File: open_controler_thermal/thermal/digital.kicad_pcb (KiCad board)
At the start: 2 copper layers, 56 x 85 mm, 6 parts, among them J1 d_o_01x10, J2 d_i_01x10, J3 Conn_02x20_Odd_Even, J4 Conn_01x02

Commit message: trabajando en openControllerDigital
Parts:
- removed the J1 at (75.7, 82.8)
- added C1: 10nF, Capacitor_SMD:C_1206_3216Metric_Pad1.42x1.75mm_HandSolder, F.Cu at (109.0, 138.3)
- added C10: 10nF, Capacitor_SMD:C_1206_3216Metric_Pad1.42x1.75mm_HandSolder, F.Cu at (85.4, 74.2)
- added C11: 10nF, Capacitor_SMD:C_1206_3216Metric_Pad1.42x1.75mm_HandSolder, F.Cu at (90.0, 62.2)
- added C12: 10nF, Capacitor_SMD:C_1206_3216Metric_Pad1.42x1.75mm_HandSolder, F.Cu at (94.7, 74.1)
- added C13: 10nF, Capacitor_SMD:C_1206_3216Metric_Pad1.42x1.75mm_HandSolder, F.Cu at (99.2, 62.2)
- added C14: 10nF, Capacitor_SMD:C_1206_3216Metric_Pad1.42x1.75mm_HandSolder, F.Cu at (104.0, 74.2)
- added C15: 10nF, Capacitor_SMD:C_1206_3216Metric_Pad1.42x1.75mm_HandSolder, F.Cu at (108.5, 62.2)
- added C16: 10nF, Capacitor_SMD:C_1206_3216Metric_Pad1.42x1.75mm_HandSolder, F.Cu at (113.0, 74.2)
- added C2: 10nF, Capacitor_SMD:C_1206_3216Metric_Pad1.42x1.75mm_HandSolder, F.Cu at (79.3, 92.5)
- added C3: 10nF, Capacitor_SMD:C_1206_3216Metric_Pad1.42x1.75mm_HandSolder, F.Cu at (79.4, 97.8)
- added C4: 10nF, Capacitor_SMD:C_1206_3216Metric_Pad1.42x1.75mm_HandSolder, F.Cu at (79.4, 103.2)
- added C5: 10nF, Capacitor_SMD:C_1206_3216Metric_Pad1.42x1.75mm_HandSolder, F.Cu at (79.4, 113.9)
- added C6: 10nF, Capacitor_SMD:C_1206_3216Metric_Pad1.42x1.75mm_HandSolder, F.Cu at (79.4, 119.3)
- added C8: 10nF, Capacitor_SMD:C_1206_3216Metric_Pad1.42x1.75mm_HandSolder, F.Cu at (79.4, 108.5)
- added C9: 10nF, Capacitor_SMD:C_1206_3216Metric_Pad1.42x1.75mm_HandSolder, F.Cu at (79.3, 130.0)
- added J4: e_i_01x10, Connector_Phoenix_MC:PhoenixContact_MCV_1,5_10-G-3.5_1x10_P3.50mm_Vertical, F.Cu at (72.7, 98.4)
- added JP1: 23, Jumper:SolderJumper-2_P1.3mm_Open_RoundedPad1.0x1.5mm, F.Cu at (111.5, 96.8)
- added JP2: 19, Jumper:SolderJumper-2_P1.3mm_Open_RoundedPad1.0x1.5mm, F.Cu at (111.5, 112.0)
- added JP3: 18, Jumper:SolderJumper-2_P1.3mm_Open_RoundedPad1.0x1.5mm, F.Cu at (111.5, 114.6)
- added JP4: 05, Jumper:SolderJumper-2_P1.3mm_Open_RoundedPad1.0x1.5mm, F.Cu at (111.5, 117.1)
- added JP5: tx, Jumper:SolderJumper-2_P1.3mm_Open_RoundedPad1.0x1.5mm, B.Cu at (118.8, 118.9)
- added JP6: rx, Jumper:SolderJumper-2_P1.3mm_Open_RoundedPad1.0x1.5mm, B.Cu at (118.8, 123.2)
- added JP7: 04, Jumper:SolderJumper-2_P1.3mm_Open_RoundedPad1.0x1.5mm, F.Cu at (111.5, 124.8)
- added R1: 4k7, Resistor_SMD:R_1206_3216Metric_Pad1.42x1.75mm_HandSolder, F.Cu at (94.5, 99.3)
- added R10: 10k, Resistor_SMD:R_1206_3216Metric_Pad1.42x1.75mm_HandSolder, F.Cu at (83.5, 115.2)
- added R11: 10k, Resistor_SMD:R_1206_3216Metric_Pad1.42x1.75mm_HandSolder, F.Cu at (83.5, 120.6)
- added R12: 10k, Resistor_SMD:R_1206_3216Metric_Pad1.42x1.75mm_HandSolder, F.Cu at (83.5, 126.0)
- added R13: 10k, Resistor_SMD:R_1206_3216Metric_Pad1.42x1.75mm_HandSolder, F.Cu at (83.5, 91.2)
- added R14: 10k, Resistor_SMD:R_1206_3216Metric_Pad1.42x1.75mm_HandSolder, F.Cu at (83.5, 96.5)
- added R15: 10k, Resistor_SMD:R_1206_3216Metric_Pad1.42x1.75mm_HandSolder, F.Cu at (83.5, 101.8)
- added R16: 10k, Resistor_SMD:R_1206_3216Metric_Pad1.42x1.75mm_HandSolder, F.Cu at (83.5, 112.6)
- added R17: 10k, Resistor_SMD:R_1206_3216Metric_Pad1.42x1.75mm_HandSolder, F.Cu at (83.5, 117.9)
- added R18: 10k, Resistor_SMD:R_1206_3216Metric_Pad1.42x1.75mm_HandSolder, F.Cu at (83.5, 123.3)
- added R19: 4k7, Resistor_SMD:R_1206_3216Metric_Pad1.42x1.75mm_HandSolder, F.Cu at (94.5, 107.0)
- added R2: 4k7, Resistor_SMD:R_1206_3216Metric_Pad1.42x1.75mm_HandSolder, F.Cu at (94.5, 101.9)
- added R20: 4k7, Resistor_SMD:R_1206_3216Metric_Pad1.42x1.75mm_HandSolder, F.Cu at (94.6, 117.1)
- added R21: 4k7, Resistor_SMD:R_1206_3216Metric_Pad1.42x1.75mm_HandSolder, F.Cu at (94.5, 119.6)
- added R22: 4k7, Resistor_SMD:R_1206_3216Metric_Pad1.42x1.75mm_HandSolder, F.Cu at (94.5, 122.9)
- added R23: 4k7, Resistor_SMD:R_1206_3216Metric_Pad1.42x1.75mm_HandSolder, F.Cu at (94.5, 126.4)
- added R24: 4k7, Resistor_SMD:R_1206_3216Metric_Pad1.42x1.75mm_HandSolder, F.Cu at (94.5, 129.8)
- added R25: 4k7, Resistor_SMD:R_1206_3216Metric_Pad1.42x1.75mm_HandSolder, F.Cu at (119.9, 132.3)
- added R26: 4k7, Resistor_SMD:R_1206_3216Metric_Pad1.42x1.75mm_HandSolder, F.Cu at (119.9, 129.8)
- added R27: 10k, Resistor_SMD:R_1206_3216Metric_Pad1.42x1.75mm_HandSolder, F.Cu at (83.5, 109.9)
- added R28: 10k, Resistor_SMD:R_1206_3216Metric_Pad1.42x1.75mm_HandSolder, F.Cu at (83.5, 131.4)
- added R29: 10k, Resistor_SMD:R_1206_3216Metric_Pad1.42x1.75mm_HandSolder, F.Cu at (84.1, 78.3)
- added R3: 4k7, Resistor_SMD:R_1206_3216Metric_Pad1.42x1.75mm_HandSolder, F.Cu at (94.5, 104.4)
- added R30: 10k, Resistor_SMD:R_1206_3216Metric_Pad1.42x1.75mm_HandSolder, F.Cu at (88.7, 66.3)
- added R31: 10k, Resistor_SMD:R_1206_3216Metric_Pad1.42x1.75mm_HandSolder, F.Cu at (93.4, 78.3)
- added R32: 10k, Resistor_SMD:R_1206_3216Metric_Pad1.42x1.75mm_HandSolder, F.Cu at (97.9, 66.3)
- added R33: 10k, Resistor_SMD:R_1206_3216Metric_Pad1.42x1.75mm_HandSolder, F.Cu at (102.7, 78.3)
- added R34: 10k, Resistor_SMD:R_1206_3216Metric_Pad1.42x1.75mm_HandSolder, F.Cu at (107.2, 66.3)
- added R35: 10k, Resistor_SMD:R_1206_3216Metric_Pad1.42x1.75mm_HandSolder, F.Cu at (83.5, 107.2)
- added R36: 10k, Resistor_SMD:R_1206_3216Metric_Pad1.42x1.75mm_HandSolder, F.Cu at (83.5, 128.7)
- added R37: 10k, Resistor_SMD:R_1206_3216Metric_Pad1.42x1.75mm_HandSolder, F.Cu at (86.7, 78.3)
- added R38: 10k, Resistor_SMD:R_1206_3216Metric_Pad1.42x1.75mm_HandSolder, F.Cu at (91.3, 66.3)
- added R39: 10k, Resistor_SMD:R_1206_3216Metric_Pad1.42x1.75mm_HandSolder, F.Cu at (96.0, 78.3)
- added R4: 4k7, Resistor_SMD:R_1206_3216Metric_Pad1.42x1.75mm_HandSolder, F.Cu at (94.5, 109.5)
- added R40: 10k, Resistor_SMD:R_1206_3216Metric_Pad1.42x1.75mm_HandSolder, F.Cu at (100.6, 66.3)
- added R41: 10k, Resistor_SMD:R_1206_3216Metric_Pad1.42x1.75mm_HandSolder, F.Cu at (105.3, 78.3)
- added R42: 10k, Resistor_SMD:R_1206_3216Metric_Pad1.42x1.75mm_HandSolder, F.Cu at (109.8, 66.3)
- added R43: 4k7, Resistor_SMD:R_1206_3216Metric_Pad1.42x1.75mm_HandSolder, F.Cu at (120.0, 127.3)
- added R5: 4k7, Resistor_SMD:R_1206_3216Metric_Pad1.42x1.75mm_HandSolder, F.Cu at (94.5, 112.0)
- added R51: 10k, Resistor_SMD:R_1206_3216Metric_Pad1.42x1.75mm_HandSolder, F.Cu at (111.7, 78.3)
- added R59: 10k, Resistor_SMD:R_1206_3216Metric_Pad1.42x1.75mm_HandSolder, F.Cu at (114.3, 78.3)
- added R6: 4k7, Resistor_SMD:R_1206_3216Metric_Pad1.42x1.75mm_HandSolder, F.Cu at (94.5, 114.6)
- added R7: 10k, Resistor_SMD:R_1206_3216Metric_Pad1.42x1.75mm_HandSolder, F.Cu at (83.5, 93.8)
- added R8: 10k, Resistor_SMD:R_1206_3216Metric_Pad1.42x1.75mm_HandSolder, F.Cu at (83.5, 99.2)
- added R9: 10k, Resistor_SMD:R_1206_3216Metric_Pad1.42x1.75mm_HandSolder, F.Cu at (83.5, 104.5)
- added U1: ESP32_NODEMCU_OS, Espressif:ESP32-DevKitC, F.Cu at (89.1, 94.3)
- C7: value 10 -> 10nF; moved to F.Cu
- D1: footprint Diode_SMD:D_2114_3652Metric -> Digital:D_2114_3652Metric; moved to F.Cu
- J2: value d_i_01x10 -> Conn_02x20_Odd_Even; footprint Connector_Phoenix_MC:PhoenixContact_MCV_1,5_10-G-3.5_1x10_P3.50mm_Vertical -> Connector_PinHeader_2.54mm:PinHeader_2x20_P2.54mm_Vertical
- J3: value Conn_02x20_Odd_Even -> a_i_01x10; footprint Connector_PinHeader_2.54mm:PinHeader_2x20_P2.54mm_Vertical -> Connector_Phoenix_MC:PhoenixContact_MCV_1,5_10-G-3.5_1x10_P3.50mm_Vertical
- moved J3 100.7 mm to (72.7, 136.4), turned to 90 degrees
- moved J2 58.6 mm to (121.5, 65.7), turned to 0 degrees
- moved J1 45.1 mm to (83.0, 139.7), turned to 180 degrees
- moved D1 42.0 mm to (94.2, 136.7), turned to 270 degrees
- moved C7 31.0 mm to (79.3, 124.6)
- renumbered J4 to J1
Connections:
- net di20 renamed Net-(J2-Pad1)
- net di32 renamed Net-(J2-Pad7)
- C7 pad 1: 5v -> jA25
- C7 pad 2: GND_1 -> GND
- J1 pad 2: GND_1 -> GND
- J2 pad 10: GND_1 -> RXD
- J2 pad 2: di21 -> 5v_1
- J2 pad 3: di22 -> SDA
- J2 pad 4: gi2 -> 5v_1
- J2 pad 5: di30 -> SCL
- J2 pad 6: di31 -> GND
- J2 pad 8: gi3 -> TXD
- J2 pad 9: 5v_1 -> GND
- J3 pad 1: Net-(J3-Pad1) -> GND
- J3 pad 10: Net-(J3-Pad10) -> 3v3
- J3 pad 2: 5v_1 -> jA26
- J3 pad 3: Net-(J3-Pad3) -> jA25
- J3 pad 4: 5v_1 -> jA33
- J3 pad 5: Net-(J3-Pad5) -> jA32
- J3 pad 6: GND_1 -> jA35
- J3 pad 7: Net-(J3-Pad7) -> jA34
- J3 pad 8: Net-(J3-Pad8) -> jA39
- J3 pad 9: GND_1 -> jA36
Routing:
- net D13: track 0.00 -> 71.8 mm
- net D14: track 0.00 -> 66.8 mm
- net D02: track 0.00 -> 65.2 mm
- net jD00: track 0.00 -> 62.0 mm
- net o04: track 0.00 -> 60.4 mm
- net jD15: track 0.00 -> 58.6 mm
- net D12: track 0.00 -> 56.9 mm
- net SDA: track 0.00 -> 54.1 mm
- net RXD: track 0.00 -> 52.1 mm
- net D27: track 0.00 -> 51.8 mm
- net D00: track 0.00 -> 51.5 mm
- net D15: track 0.00 -> 51.1 mm
- net jD12: track 0.00 -> 50.0 mm
- net TXD: track 0.00 -> 49.6 mm
- net o05: track 0.00 -> 49.0 mm
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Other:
- board size 56 x 85 mm -> 195.4 x 89.1 mm

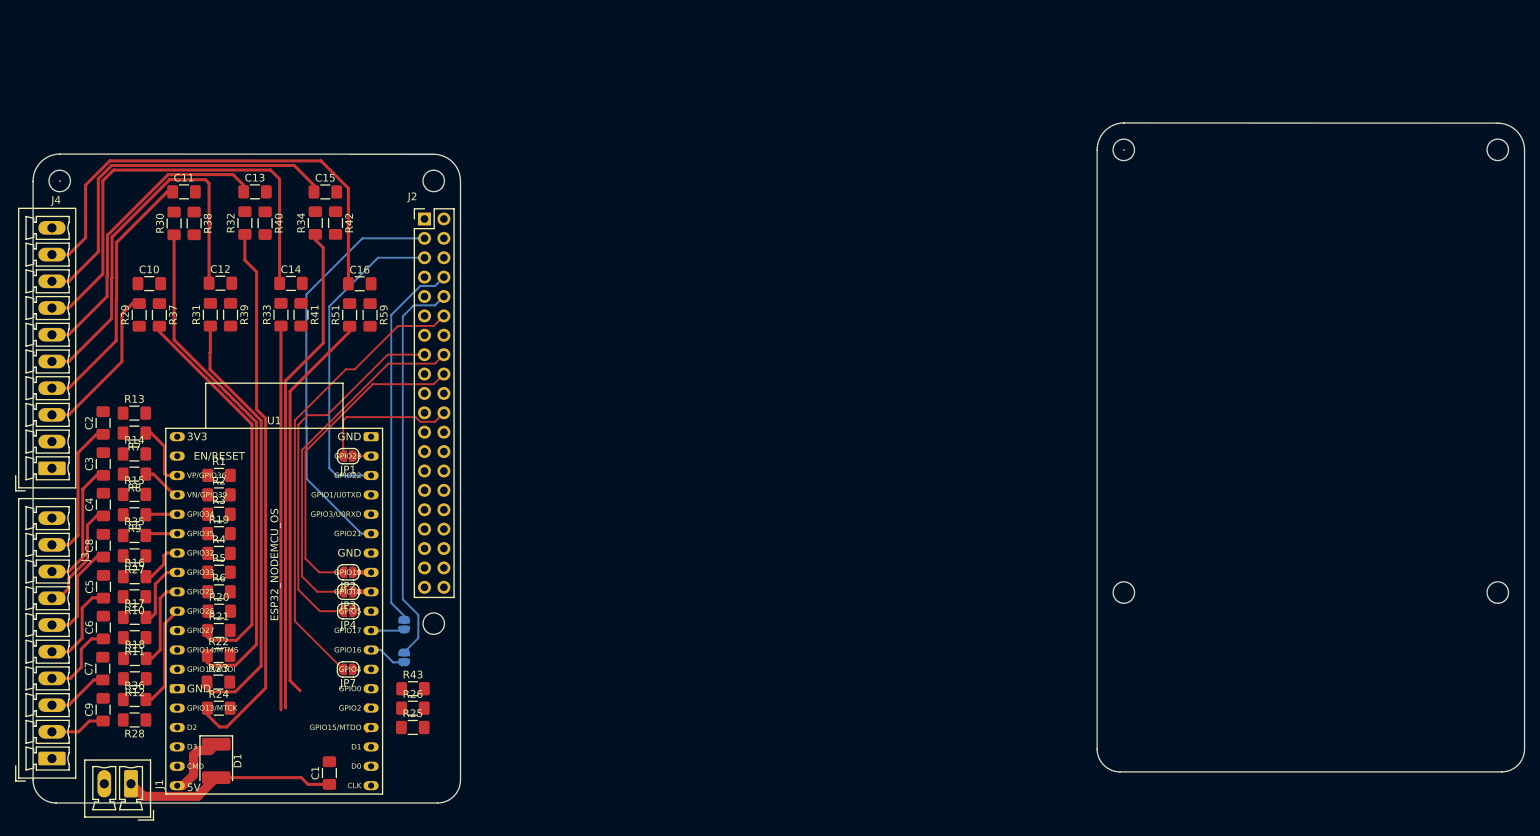
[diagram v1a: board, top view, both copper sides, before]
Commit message: version fabricada de open_controles_thermal
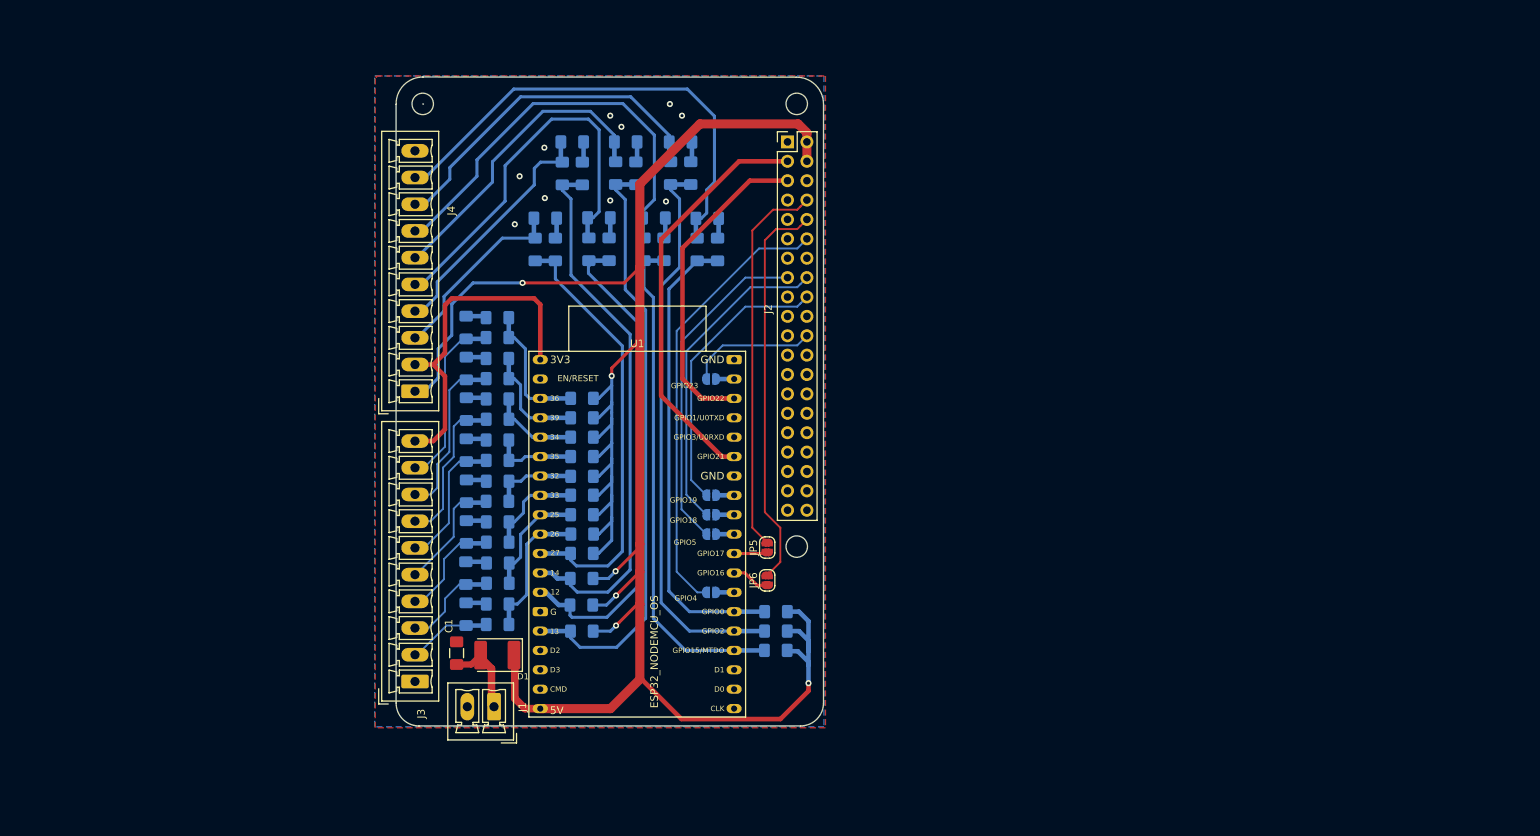
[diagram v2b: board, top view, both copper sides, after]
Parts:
- C10, C11, C12, C13, C14, C15, C16, C2, C3, C4, C5, C6, C7, C8, C9, JP1, JP2, JP3, JP4, JP7, R1, R10, R11, R12, R13, R14, R15, R16, R17, R18, R19, R2, R20, R21, R22, R23, R24, R25, R26, R27, R28, R29, R3, R30, R31, R32, R33, R34, R35, R36, R37, R38, R39, R4, R40, R41, R42, R43, R5, R51, R59, R6, R7, R8, R9: moved to B.Cu
- JP5, JP6: moved to F.Cu
- moved C10 52.6 mm to (137.3, 65.6)
- moved R37 52.6 mm to (138.6, 69.7)
- moved R29 52.6 mm to (136.0, 69.7)
- moved C11 51.3 mm to (140.8, 55.6)
- moved R30 51.3 mm to (139.5, 59.8)
- moved R38 51.3 mm to (142.1, 59.8)
- moved R31 50.3 mm to (143.0, 69.7)
- moved C12 50.3 mm to (144.3, 65.6)
- moved R39 50.3 mm to (145.6, 69.7)
- moved C2 49.2 mm to (126.9, 80.0)
- moved C5 49.2 mm to (127.0, 101.4)
- moved C7 49.2 mm to (126.9, 112.1)
- moved C9 49.2 mm to (126.9, 117.5)
- moved R10 49.2 mm to (131.0, 102.7)
- moved R11 49.2 mm to (131.1, 108.1)
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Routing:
- net 5v_1: track 8.88 -> 295.2 mm, vias 0 -> 6
- net 3v3: track 0.00 -> 44.9 mm
- net GND: track 0.00 -> 40.3 mm, vias 0 -> 10
- net 5v: track 28.1 -> 11.1 mm
- net D15: track 51.1 -> 66.3 mm
- net D00: track 51.5 -> 61.1 mm
- net A39: track 5.25 -> 14.7 mm
- net A36: track 8.51 -> 17.5 mm
- net D02: track 65.2 -> 74.0 mm
- net D12: track 56.9 -> 64.6 mm
- net A34: track 4.13 -> 11.7 mm
- net A35: track 4.22 -> 11.0 mm
- net D13: track 71.8 -> 77.9 mm
- net jA34: track 14.6 -> 20.4 mm
- net D27: track 51.8 -> 57.1 mm
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- added copper zone on B.Cu, net GND
- added copper zone on F.Cu, net GND
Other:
- board size 195.4 x 89.1 mm -> 56 x 85 mm

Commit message: ecotherm. actualizacion de los conectores phenix
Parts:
- J1: footprint Connector_Phoenix_MC:PhoenixContact_MCV_1,5_2-G-3.5_1x02_P3.50mm_Vertical -> Connector_Phoenix_MC:PhoenixContact_MC_1,5_2-G-3.5_1x02_P3.50mm_Horizontal
- J3, J4: footprint Connector_Phoenix_MC:PhoenixContact_MCV_1,5_10-G-3.5_1x10_P3.50mm_Vertical -> Connector_Phoenix_MC:PhoenixContact_MC_1,5_10-G-3.5_1x10_P3.50mm_Horizontal
- moved J4 31.5 mm to (120.2, 56.8), turned to 270 degrees
- moved J3 31.5 mm to (120.2, 94.8), turned to 270 degrees
- moved J1 3.50 mm to (127.1, 129.6), turned to 0 degrees
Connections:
- J1 pad 1: 5v -> GND
- J1 pad 2: GND -> 5v
- J3 pad 1: GND -> 3v3
- J3 pad 10: 3v3 -> GND
- J3 pad 2: jA26 -> jA36
- J3 pad 3: jA25 -> jA39
- J3 pad 4: jA33 -> jA34
- J3 pad 5: jA32 -> jA35
- J3 pad 6: jA35 -> jA32
- J3 pad 7: jA34 -> jA33
- J3 pad 8: jA39 -> jA25
- J3 pad 9: jA36 -> jA26
- J4 pad 1: 5v_1 -> GND
- J4 pad 10: GND -> 5v_1
- J4 pad 2: 3v3 -> jD00
- J4 pad 3: jD27 -> jD02
- J4 pad 4: jD14 -> jD15
- J4 pad 5: jD12 -> jD13
- J4 pad 6: jD13 -> jD12
- J4 pad 7: jD15 -> jD14
- J4 pad 8: jD02 -> jD27
- J4 pad 9: jD00 -> 3v3

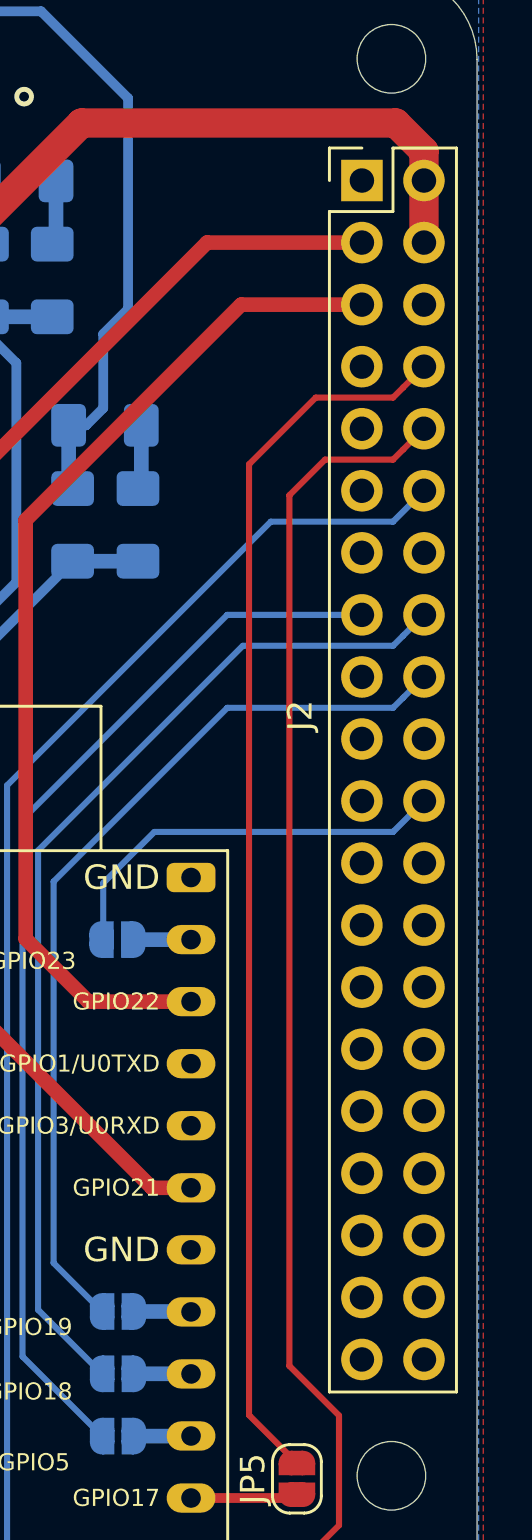
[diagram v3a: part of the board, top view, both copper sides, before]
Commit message: ecotherm. actualizacion del conector del bus
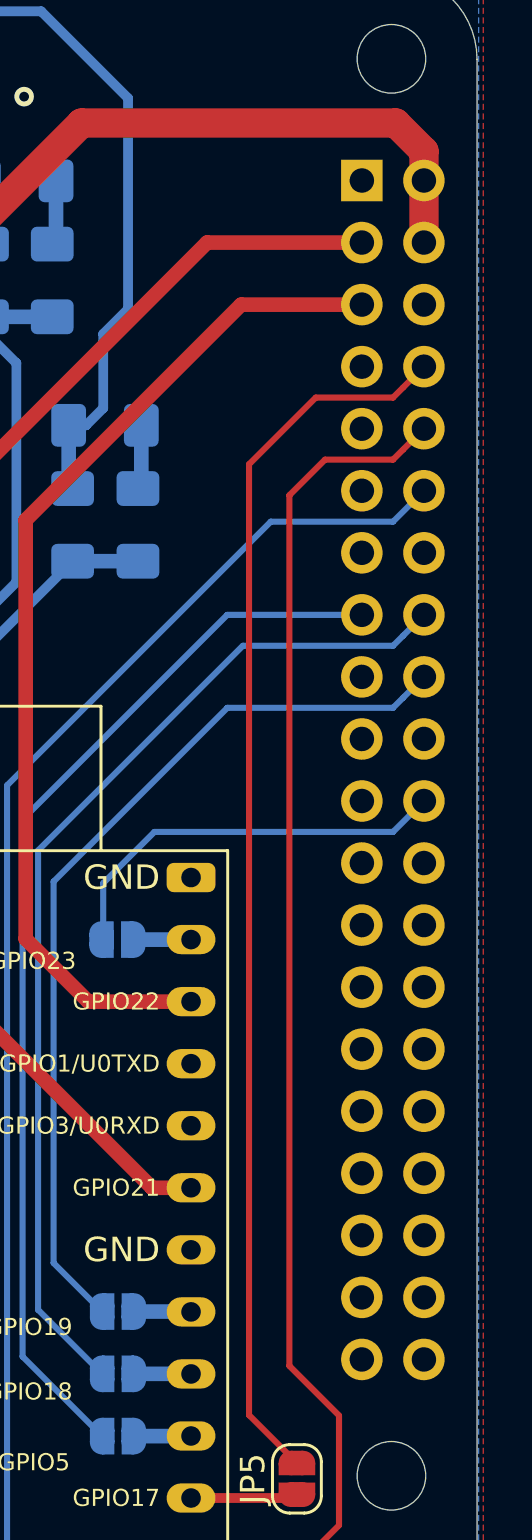
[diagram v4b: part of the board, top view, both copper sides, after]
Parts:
- J2: footprint Connector_PinHeader_2.54mm:PinHeader_2x20_P2.54mm_Vertical -> Connector_PinSocket_2.54mm:PinSocket_2x20_P2.54mm_Vertical; moved to B.Cu
- turned J2 to 180 degrees
